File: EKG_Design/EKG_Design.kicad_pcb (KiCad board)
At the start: 2 copper layers, 41.4 x 22.6 mm, 55 parts, among them IC101 OPA2156IDGKR, IC102 OPA2156IDGKR, IC103 OPA2156IDGKR, IC104 INA826AIDR_/_SOIC8, J100 Conn_01x02_Pin, J101 Conn_01x02_Pin, J102 Conn_01x02_Pin, J103 Conn_01x02_Pin, J104 Conn_01x03_Pin, Q200 BC848C

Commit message: Finished ECG Routing
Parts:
- moved C104 4.63 mm to (103.0, 78.3), turned to 90 degrees
- moved C105 4.19 mm to (106.2, 79.5), turned to 90 degrees
- moved J100 1.85 mm to (102.3, 69.6)
- moved H102 1.47 mm to (94.9, 87.4)
- moved J101 1.41 mm to (94.9, 74.3)
- moved J102 1.41 mm to (94.9, 80.5)
- moved H103 1.38 mm to (94.9, 70.0)
- moved R108 0.51 mm to (99.0, 83.1)
- moved R109 0.51 mm to (97.4, 83.1)
- moved C102 0.51 mm to (100.5, 83.1)
- moved R102 0.44 mm to (115.3, 70.9)
- moved C106 0.40 mm to (107.7, 79.5)
- moved C100 0.31 mm to (115.3, 74.2)
- moved C107 0.31 mm to (115.3, 75.7)
- moved R103 0.31 mm to (115.3, 72.7)
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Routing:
- net 5V0_Analog: track 0.00 -> 63.1 mm, vias 0 -> 4
- net 5N0_Analog: track 0.00 -> 56.5 mm, vias 0 -> 2
- net GND: track 0.00 -> 38.8 mm, vias 0 -> 10
- net Net-(D200-C): track 0.00 -> 17.6 mm
- net /EKG-Details/EKG+: track 0.00 -> 16.6 mm, vias 0 -> 2
- net ECG_Out: track 0.00 -> 16.6 mm
- net /EKG-Details/VCM: track 0.00 -> 14.3 mm, vias 0 -> 2
- net /EKG-Details/EKG-: track 0.00 -> 12.4 mm
- net Net-(IC102B--): track 0.00 -> 11.2 mm
- net /EKG-Details/Shield+: track 0.00 -> 9.79 mm
- net /EKG-Details/Shield-: track 0.00 -> 9.53 mm
- net Net-(J100-Pin_2): track 0.00 -> 8.69 mm
- net Net-(IC104-Ref): track 0.00 -> 8.51 mm
- net Net-(IC101A-+): track 0.00 -> 7.24 mm
- net Net-(J101-Pin_1): track 0.00 -> 6.22 mm
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- added copper zone on B.Cu, net GND
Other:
- board size 41.4 x 22.6 mm -> 40.7 x 23.2 mm

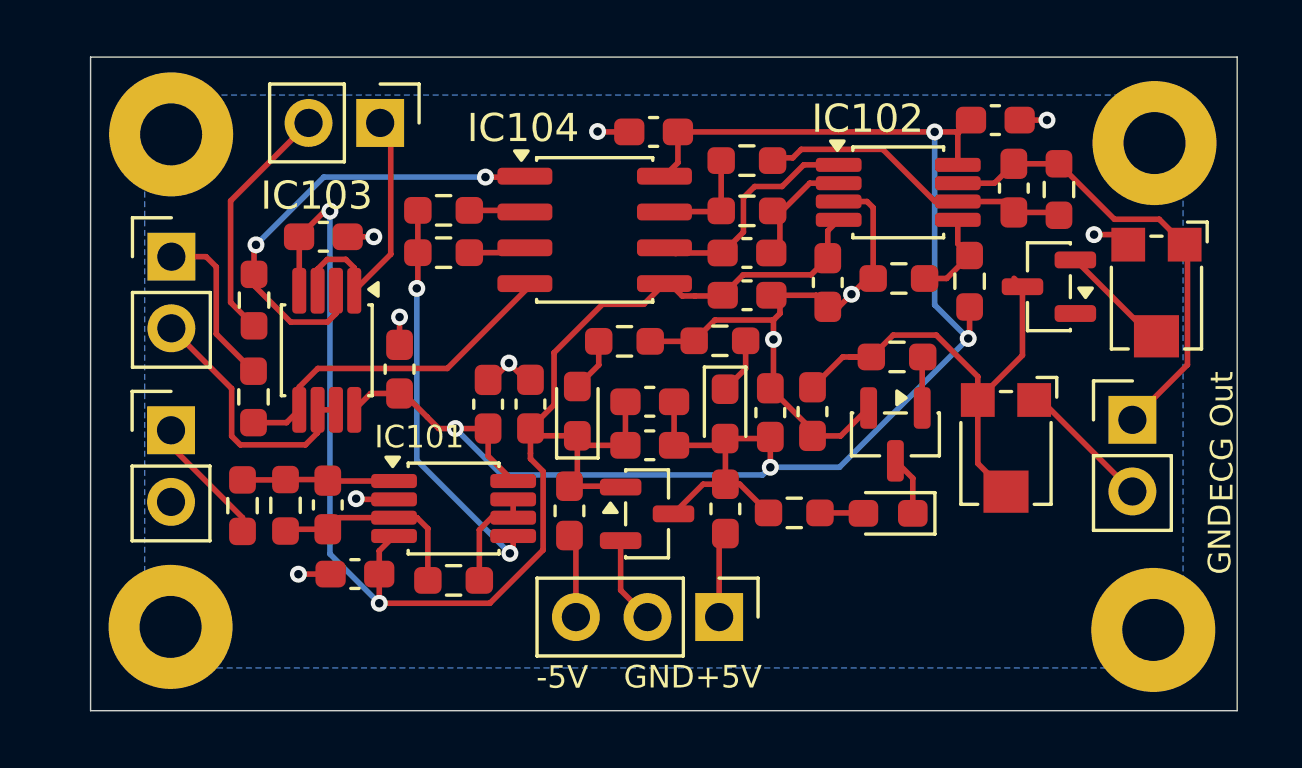
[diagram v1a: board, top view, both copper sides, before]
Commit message: adjusted board properties and added manifest items
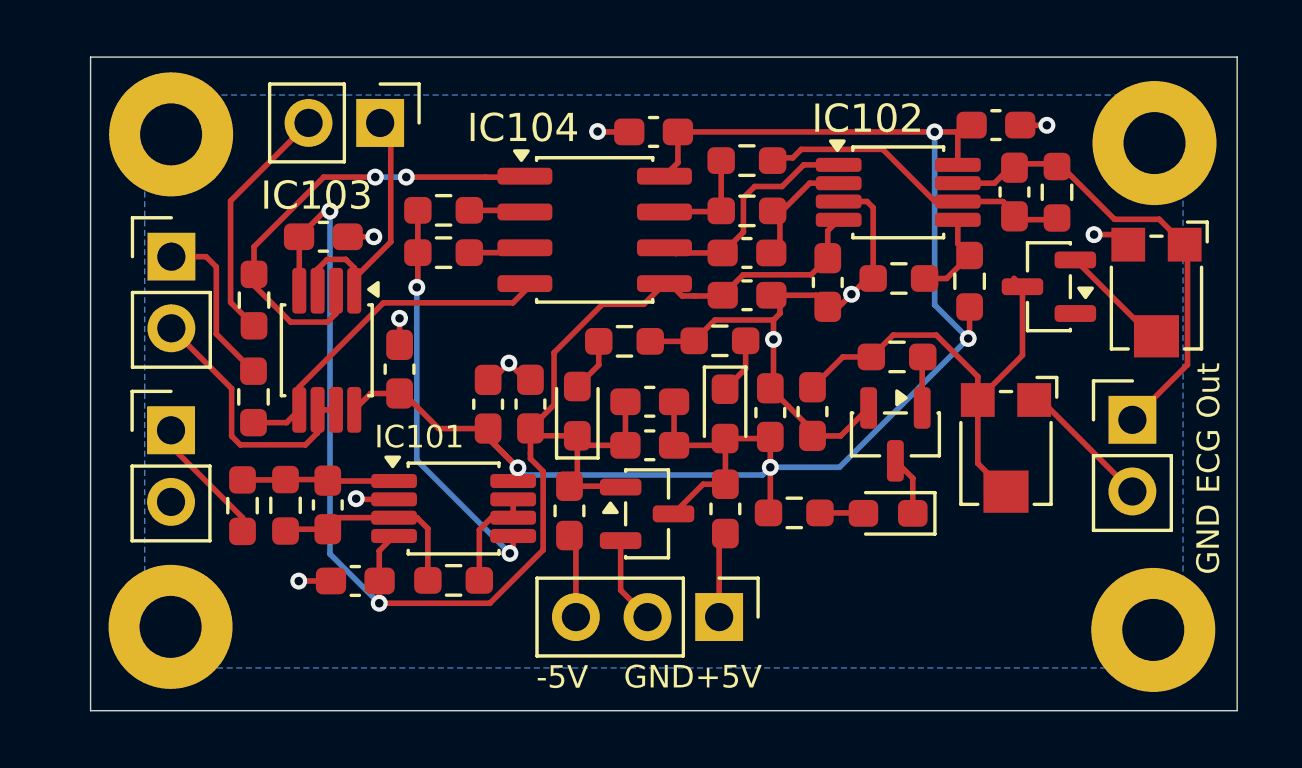
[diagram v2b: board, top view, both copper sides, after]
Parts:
- moved C112 0.24 mm to (101.5, 85.8)
- moved C111 0.18 mm to (124.2, 69.6)
- moved C101 0.14 mm to (124.8, 72.0)
- moved R104 0.12 mm to (126.3, 72.0)
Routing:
- net Net-(D200-C): track 17.6 -> 16.8 mm
- net 5V0_Analog: track 63.1 -> 62.4 mm
